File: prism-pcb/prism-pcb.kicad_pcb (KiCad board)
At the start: 4 copper layers, 40 x 40 mm, 41 parts, among them J301 FFC_P1mm_BOT_RA_SMD, J401 Molex_Pico-SPOX_Horizontal, M301 Fan_5VDC_25x25x8mm, U301 TPSM365R6V5RDNR, U402 TMC5130A-TA, X401 16MHz

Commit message: tmc5130-uart -> prism-pcb
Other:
- board text added: "https://github.com/janelia-kicad/prism-pcb"
- board text added: "prism-pcb v1.0 2024/05 48V 1.6A RMS 2.2A PEAK"
- board text removed: "https://github.com/janelia-kicad/tmc5130-uart"
- board text removed: "tmc5130-uart v1.0 2024/05 48V 1.6A RMS 2.2A PEAK"
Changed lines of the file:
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@@
   (paper "A4")
   (title_block
-    (title "tmc5130-uart")
+    (title "prism-pcb")
     (date "2024-07-11")
     (rev "1.0")
@@
     (effects (font (size 1 0.6) (thickness 0.15) bold))
   )
-  (gr_text "tmc5130-uart\nv1.0 2024/05\n48V 1.6A RMS 2.2A PEAK" (at 158.4 116.1) (layer "F.SilkS")
+  (gr_text "prism-pcb\nv1.0 2024/05\n48V 1.6A RMS 2.2A PEAK" (at 158.4 116.1) (layer "F.SilkS")
     (effects (font (size 1 0.6) (thickness 0.15) bold))
   )
-  (gr_text "https://github.com/janelia-kicad/tmc5130-uart" (at 152.4 119.6) (layer "F.SilkS")
+  (gr_text "https://github.com/janelia-kicad/prism-pcb" (at 152.4 119.6) (layer "F.SilkS")
     (effects (font (size 1 0.6) (thickness 0.15) bold))
   )

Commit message: Initial footprint layout
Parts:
- removed C305: 1uF_25V, Janelia:C_0402_1005Metric
- removed C413: 0.1uF_100V, Janelia:C_0402_1005Metric
- removed C414, C415: 2.2uF_100V, Janelia:C_0805_2012Metric
- removed C416, C417: 100uF_50V, Janelia:CAP_EEEFTH101XAV
- removed M301: Fan_5VDC_25x25x8mm, Janelia:FAN_5VDC_25x25x8mm
- removed R302: 120, Janelia:R_0402_1005Metric
- removed U402: TMC5130A-TA, Janelia:TQFP-48-1EP_7x7mm_P0.5mm_EP5x5mm_ThermalVias
- added U401: TMC5130A-TA, Janelia:TQFP-48-1EP_7x7mm_P0.5mm_EP5x5mm_ThermalVias, F.Cu at (152.4, 101.6)
- C301, J301, J401, U301: moved to F.Cu
- C302: value 1uF_25V -> 0.1uF_100V; moved to F.Cu
- C304: value 0.1uF_100V -> 1uF_25V
- C407: value 2.2uF_35V -> 0.1uF_100V
- C408: value 0.1uF_100V -> 2.2uF_100V; footprint Janelia:C_0402_1005Metric -> Janelia:C_0805_2012Metric
- C409, C412: value 0.22uF_25V -> 100uF_50V; footprint Janelia:C_0402_1005Metric -> Janelia:CAP_EEEFTH101XAV
- C410: value 0.22uF_25V -> 0.1uF_100V
- C411: value 0.22uF_25V -> 2.2uF_100V; footprint Janelia:C_0402_1005Metric -> Janelia:C_0805_2012Metric
- R301: value 100k -> 100
- moved C303 35.0 mm to (149.4, 113.6), turned to -90 degrees
- moved C304 28.5 mm to (141.4, 113.6), turned to -90 degrees
- moved R403 19.2 mm to (151.4, 111.6), turned to -90 degrees
- moved C405 18.3 mm to (160.4, 92.6), turned to 90 degrees
- moved C411 17.1 mm to (162.4, 110.6)
- moved C412 16.5 mm to (157.4, 116.6), turned to 0 degrees
- moved C409 14.8 mm to (155.4, 88.6), turned to 90 degrees
- moved C403 14.0 mm to (155.4, 94.6)
- moved C402 13.0 mm to (157.4, 96.6), turned to 90 degrees
- moved C408 12.7 mm to (145.4, 85.6)
- moved C407 11.7 mm to (149.4, 84.6)
- moved C406 8.94 mm to (159.4, 90.6), turned to 0 degrees
- moved C302 8.56 mm to (148.4, 110.6), turned to 0 degrees
- moved R301 8.06 mm to (141.4, 97.6), turned to 90 degrees
- moved C301 6.80 mm to (143.4, 109.6), turned to 180 degrees
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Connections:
- C302 pad 1: /interface/VDD -> /VM
- C303 pad 1: /VIO -> /interface/VCC
- C304 pad 1: /VM -> /VIO
- C407 pad 1: /tmc5130/12VOUT -> /VM
- C409 pad 1: /tmc5130/CA1 -> /VM
- C409 pad 2: /tmc5130/BMA1 -> /GND
- C410 pad 1: /tmc5130/CA2 -> /VM
- C410 pad 2: /tmc5130/BMA2 -> /GND
- C411 pad 1: /tmc5130/CB1 -> /VM
- C411 pad 2: /tmc5130/BMB1 -> /GND
- C412 pad 1: /tmc5130/CB2 -> /VM
- C412 pad 2: /tmc5130/BMB2 -> /GND
- R301 pad 1: /interface/PGOOD -> /SWP
- R301 pad 2: /VIO -> /SWN
- R402 pad 1: unconnected-(R402-Pad1) -> /tmc5130/BRA
- R402 pad 2: unconnected-(R402-Pad2) -> /GND
- R403 pad 1: unconnected-(R403-Pad1) -> /tmc5130/BRB
- R403 pad 2: unconnected-(R403-Pad2) -> /GND
- U301 pad 1: /interface/PGOOD -> unconnected-(U301-PGOOD-Pad1)
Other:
- board text added: "prism-pcb v1.0 2024/07 46V 1.64A RMS"
- board text removed: "+"
- board text removed: "-"
- board text removed: "48V"
- board text removed: "FAN"
- board text removed: "GND"
- board text removed: "GRN"
- board text removed: "Molex 0874380243"
- board text removed: "Molex 0874380443"
- board text removed: "Molex 5015680207"
- board text removed: "Molex 5055680281 Fan 255M"
- board text removed: "RED"
- board text removed: "REFL"
- board text removed: "TMC5160 POWER"
- board text removed: "YEL"
- board text removed: "prism-pcb v1.0 2024/05 48V 1.6A RMS 2.2A PEAK"

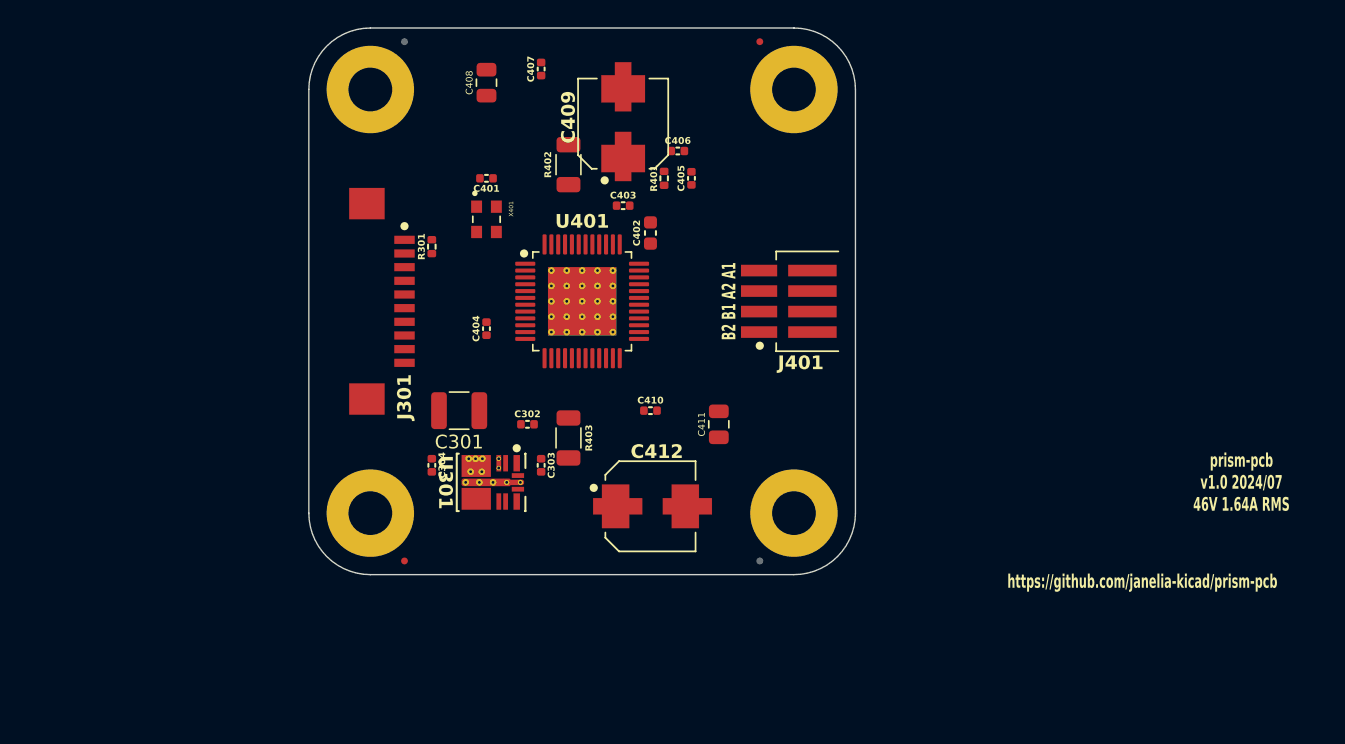
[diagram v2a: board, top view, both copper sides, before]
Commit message: Rearrange footprints
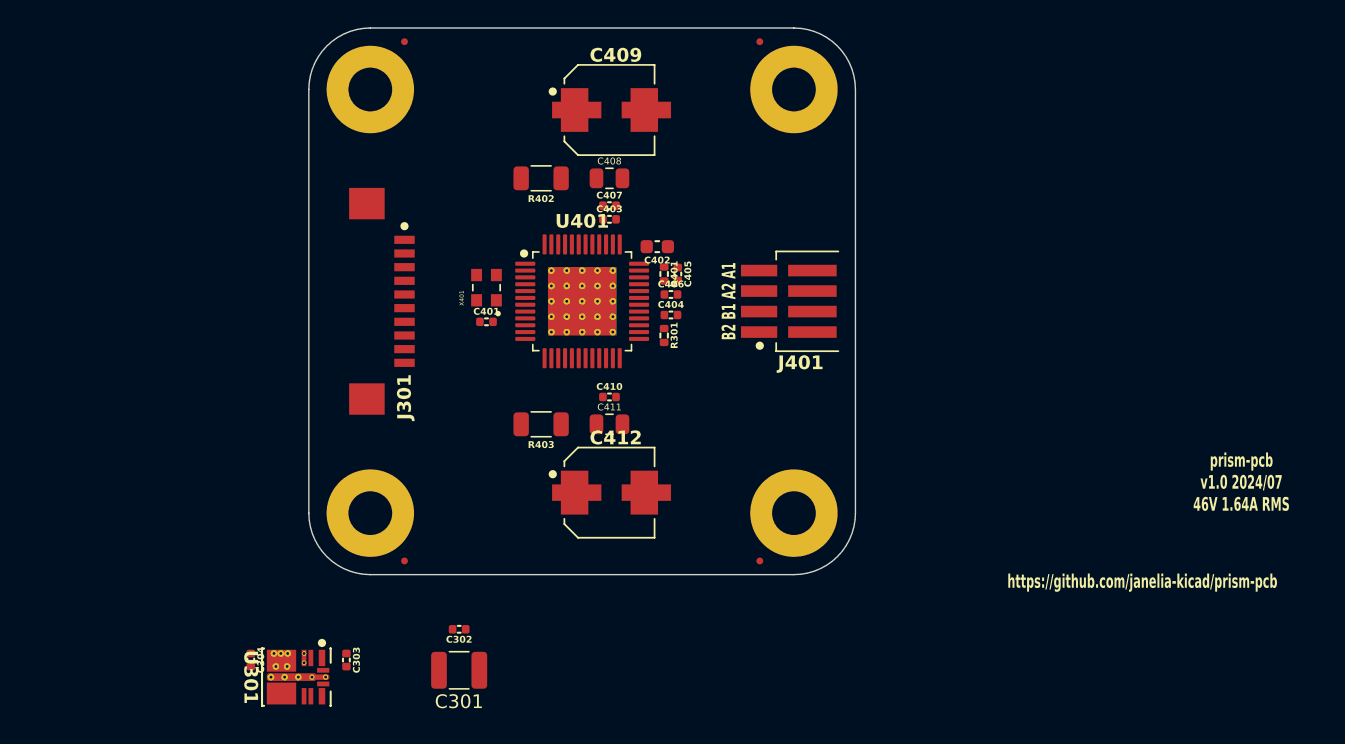
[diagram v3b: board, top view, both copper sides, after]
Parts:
- FID201, FID203: moved to F.Cu
- moved C303 20.2 mm to (135.2, 127.8)
- moved U301 20.2 mm to (131.4, 129.1)
- moved C304 19.5 mm to (128.2, 127.8)
- moved C301 19.0 mm to (143.4, 128.6)
- moved R301 18.2 mm to (158.4, 104.1), turned to -90 degrees
- moved C302 15.8 mm to (143.4, 125.6), turned to 180 degrees
- moved C404 13.5 mm to (158.9, 102.6), turned to 0 degrees
- moved C408 11.4 mm to (154.4, 92.6), turned to 0 degrees
- moved C407 11.2 mm to (154.4, 94.6), turned to 0 degrees
- moved C406 10.5 mm to (158.9, 101.1)
- moved C401 10.5 mm to (145.4, 103.1), turned to 0 degrees
- moved C411 8.00 mm to (154.4, 110.6), turned to 0 degrees
- moved C405 7.07 mm to (159.4, 99.6), turned to -90 degrees
- moved R401 7.00 mm to (158.4, 99.6), turned to -90 degrees
- moved X401 5.00 mm to (145.4, 100.6), turned to 90 degrees
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
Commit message: Place all footprints
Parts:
- added M301: Fan_5VDC_25x25x8mm, Janelia:FAN_5VDC_25x25x8mm, F.Cu at (152.4, 101.6)
- moved C304 29.4 mm to (147.9, 106.1), turned to 0 degrees
- moved U301 26.4 mm to (144.4, 106.1), turned to 180 degrees
- moved C303 20.7 mm to (141.4, 108.1)
- moved C302 19.0 mm to (147.9, 107.1), turned to 0 degrees
- moved C301 15.4 mm to (146.9, 113.6)
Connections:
- net /VIO renamed /+5V
- net /VM renamed /VAA
